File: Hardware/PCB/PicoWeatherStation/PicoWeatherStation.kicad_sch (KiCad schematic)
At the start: 42 parts, among them J1 TOUCH_PANEL, J2 LCD_BL, Q1 AO3400A, SW1 SW_PICO_RST, U1 Pico, U2 XPT2046

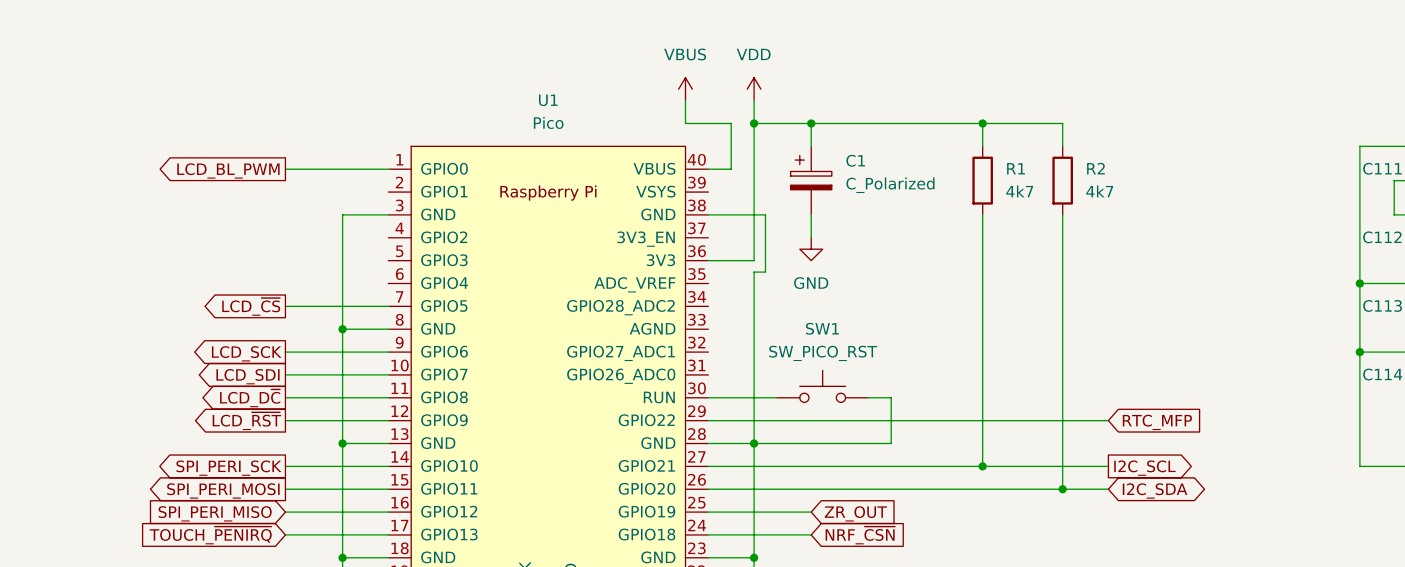
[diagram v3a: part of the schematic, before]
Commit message: PCB: wire-up the keyboard
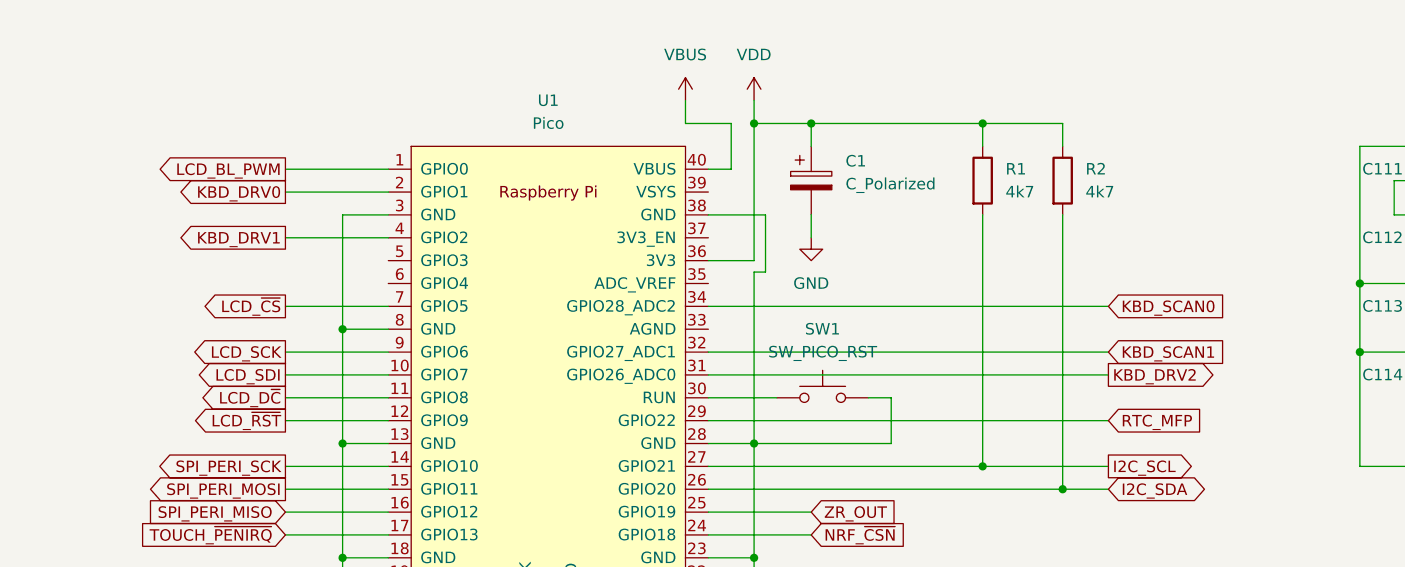
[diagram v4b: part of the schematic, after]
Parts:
- U1: footprint RPi_Pico:RPi_Pico_SMD -> PicoWeatherStation:RPi_PicoW_SMD
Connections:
- net KBD_DRV0: now reaches U1.2 (GPIO1)
- net KBD_DRV2: now reaches U1.31 (GPIO26_ADC0)
- net KBD_SCAN1: now reaches U1.32 (GPIO27_ADC1)
- net KBD_SCAN0: now reaches U1.34 (GPIO28_ADC2)
- net KBD_DRV1: now reaches U1.4 (GPIO2)
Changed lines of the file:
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@@
+    (stroke (width 0) (type default) (color 0 0 0 0))
+  )
+  (wire (pts (xy 59.69 123.19) (xy 71.12 123.19))
     (stroke (width 0) (type default) (color 0 0 0 0))
   )
@@
     (stroke (width 0) (type default) (color 0 0 0 0))
   )
+  (wire (pts (xy 106.68 130.81) (xy 151.13 130.81))
+    (stroke (width 0) (type default) (color 0 0 0 0))
+  )
   (wire (pts (xy 252.73 105.41) (xy 257.81 105.41))
     (stroke (width 0) (type default) (color 0 0 0 0))
@@
     (stroke (width 0) (type default) (color 0 0 0 0))
   )
+  (wire (pts (xy 106.68 138.43) (xy 151.13 138.43))
+    (stroke (width 0) (type default) (color 0 0 0 0))
+  )
+  (wire (pts (xy 59.69 118.11) (xy 71.12 118.11))
+    (stroke (width 0) (type default) (color 0 0 0 0))
+  )
   (wire (pts (xy 184.15 53.34) (xy 191.77 53.34))
     (stroke (width 0) (type default) (color 0 0 0 0))
@@
   )
   (wire (pts (xy 238.76 77.47) (xy 238.76 97.79))
+    (stroke (width 0) (type default) (color 0 0 0 0))
+  )
+  (wire (pts (xy 106.68 135.89) (xy 151.13 135.89))
     (stroke (width 0) (type default) (color 0 0 0 0))
   )
@@
     (property "Intersheet References" "${INTERSHEET_REFS}" (id 0) (at 161.1631 151.0506 0)
       (effects (font (size 1.27 1.27)) (justify left) hide)
+    )
+  )
+  (global_label "KBD_DRV1" (shape output) (at 59.69 123.19 180) (fields_autoplaced)
+    (effects (font (size 1.27 1.27)) (justify right))
+    (property "Intersheet References" "${INTERSHEET_REFS}" (id 0) (at 47.6612 123.1106 0)
+      (effects (font (size 1.27 1.27)) (justify right) hide)
     )
   )
@@
     )
   )
+  (global_label "KBD_SCAN0" (shape input) (at 151.13 130.81 0) (fields_autoplaced)
+    (effects (font (size 1.27 1.27)) (justify left))
+    (property "Intersheet References" "${INTERSHEET_REFS}" (id 0) (at 164.4288 130.7306 0)
+      (effects (font (size 1.27 1.27)) (justify left) hide)
+    )
+  )
   (global_label "LCD_V0" (shape passive) (at 208.28 113.03 90) (fields_autoplaced)
     (effects (font (size 1.27 1.27)) (justify left))
@@
     )
   )
+  (global_label "KBD_DRV0" (shape output) (at 59.69 118.11 180) (fields_autoplaced)
+    (effects (font (size 1.27 1.27)) (justify right))
+    (property "Intersheet References" "${INTERSHEET_REFS}" (id 0) (at 47.6612 118.0306 0)
+      (effects (font (size 1.27 1.27)) (justify right) hide)
+    )
+  )
   (global_label "LCD_~{RST}" (shape output) (at 59.69 143.51 180) (fields_autoplaced)
     (effects (font (size 1.27 1.27)) (justify right))
@@
     )
   )
+  (global_label "KBD_DRV2" (shape output) (at 151.13 138.43 0) (fields_autoplaced)
+    (effects (font (size 1.27 1.27)) (justify left))
+    (property "Intersheet References" "${INTERSHEET_REFS}" (id 0) (at 163.1588 138.3506 0)
+      (effects (font (size 1.27 1.27)) (justify left) hide)
+    )
+  )
   (global_label "SPI_PERI_MOSI" (shape input) (at 111.76 49.53 0) (fields_autoplaced)
     (effects (font (size 1.27 1.27)) (justify left))
@@
     (effects (font (size 1.27 1.27)) (justify left))
     (property "Intersheet References" "${INTERSHEET_REFS}" (id 0) (at 278.6683 128.1906 0)
+      (effects (font (size 1.27 1.27)) (justify left) hide)
+    )
+  )
+  (global_label "KBD_SCAN1" (shape input) (at 151.13 135.89 0) (fields_autoplaced)
+    (effects (font (size 1.27 1.27)) (justify left))
+    (property "Intersheet References" "${INTERSHEET_REFS}" (id 0) (at 164.4288 135.8106 0)
       (effects (font (size 1.27 1.27)) (justify left) hide)
     )
@@
     (property "Reference" "U1" (id 0) (at 88.9 107.95 0))
     (property "Value" "Pico" (id 1) (at 88.9 110.49 0))
-    (property "Footprint" "RPi_Pico:RPi_Pico_SMD" (id 2) (at 88.9 139.7 90)
+    (property "Footprint" "PicoWeatherStation:RPi_PicoW_SMD" (id 2) (at 88.9 139.7 90)
       (effects (font (size 1.27 1.27)) hide)
     )
@@
     )
     (path "/8427f957-6735-4f61-a9c3-6b6f45bea61c"
-      (reference "U1") (unit 1) (value "Pico") (footprint "RPi_Pico:RPi_Pico_SMD")
+      (reference "U1") (unit 1) (value "Pico") (footprint "PicoWeatherStation:RPi_PicoW_SMD")
     )
     (path "/540f484c-d60b-45a7-9525-536c50565709"

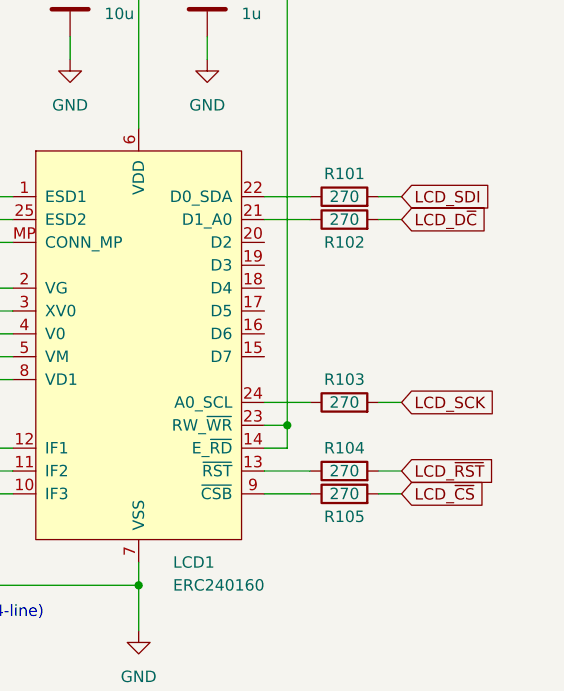
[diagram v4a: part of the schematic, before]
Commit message: PCB: optimize high speed LCD signal tracks
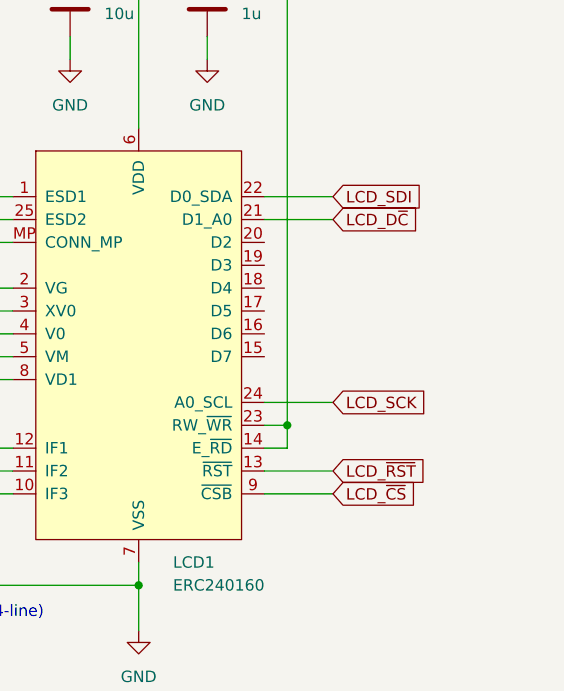
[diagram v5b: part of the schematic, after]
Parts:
- removed R101, R102, R103, R104, R105: 270, Resistor_SMD:R_0805_2012Metric_Pad1.20x1.40mm_HandSolder, symbol Device:R
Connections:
- net LCD_D~{C}: now also LCD1.21 (D1_A0)
- net LCD_SCK: now also LCD1.24 (A0_SCL)
- net LCD_SDI: now also LCD1.22 (D0_SDA)
- net LCD_~{CS}: now also LCD1.9 (~{CSB})
- net LCD_~{RST}: now also LCD1.13 (~{RST})
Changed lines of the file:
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@@
-    (stroke (width 0) (type default) (color 0 0 0 0))
-  )
-  (wire (pts (xy 265.43 107.95) (xy 267.97 107.95))
     (stroke (width 0) (type default) (color 0 0 0 0))
   )
@@
     (stroke (width 0) (type default) (color 0 0 0 0))
   )
-  (wire (pts (xy 252.73 107.95) (xy 257.81 107.95))
+  (wire (pts (xy 252.73 107.95) (xy 260.35 107.95))
     (stroke (width 0) (type default) (color 0 0 0 0))
   )
@@
     (stroke (width 0) (type default) (color 0 0 0 0))
   )
-  (wire (pts (xy 252.73 138.43) (xy 257.81 138.43))
+  (wire (pts (xy 252.73 138.43) (xy 260.35 138.43))
     (stroke (width 0) (type default) (color 0 0 0 0))
   )
@@
     (stroke (width 0) (type default) (color 0 0 0 0))
   )
-  (wire (pts (xy 265.43 128.27) (xy 267.97 128.27))
-    (stroke (width 0) (type default) (color 0 0 0 0))
-  )
   (wire (pts (xy 106.68 151.13) (xy 146.05 151.13))
     (stroke (width 0) (type default) (color 0 0 0 0))
@@
     (stroke (width 0) (type default) (color 0 0 0 0))
   )
-  (wire (pts (xy 265.43 138.43) (xy 267.97 138.43))
-    (stroke (width 0) (type default) (color 0 0 0 0))
-  )
   (wire (pts (xy 111.76 127) (xy 111.76 146.05))
     (stroke (width 0) (type default) (color 0 0 0 0))
@@
     (stroke (width 0) (type default) (color 0 0 0 0))
   )
-  (wire (pts (xy 252.73 128.27) (xy 257.81 128.27))
+  (wire (pts (xy 252.73 128.27) (xy 260.35 128.27))
     (stroke (width 0) (type default) (color 0 0 0 0))
   )
@@
     (stroke (width 0) (type default) (color 0 0 0 0))
   )
-  (wire (pts (xy 265.43 135.89) (xy 267.97 135.89))
-    (stroke (width 0) (type default) (color 0 0 0 0))
-  )
   (wire (pts (xy 113.03 120.65) (xy 113.03 127))
     (stroke (width 0) (type default) (color 0 0 0 0))
@@
     (stroke (width 0) (type default) (color 0 0 0 0))
   )
-  (wire (pts (xy 252.73 105.41) (xy 257.81 105.41))
-    (stroke (width 0) (type default) (color 0 0 0 0))
-  )
   (wire (pts (xy 69.85 22.86) (xy 69.85 25.4))
     (stroke (width 0) (type default) (color 0 0 0 0))
@@
     (stroke (width 0) (type default) (color 0 0 0 0))
   )
-  (wire (pts (xy 252.73 135.89) (xy 257.81 135.89))
+  (wire (pts (xy 252.73 135.89) (xy 260.35 135.89))
     (stroke (width 0) (type default) (color 0 0 0 0))
   )
@@
     (stroke (width 0) (type default) (color 0 0 0 0))
   )
-  (wire (pts (xy 265.43 105.41) (xy 267.97 105.41))
+  (wire (pts (xy 252.73 105.41) (xy 260.35 105.41))
     (stroke (width 0) (type default) (color 0 0 0 0))
   )
@@
     )
   )
-  (global_label "LCD_~{CS}" (shape input) (at 267.97 138.43 0) (fields_autoplaced)
-    (effects (font (size 1.27 1.27)) (justify left))
-    (property "Intersheet References" "${INTERSHEET_REFS}" (id 0) (at 277.3983 138.3506 0)
+  (global_label "LCD_~{CS}" (shape input) (at 260.35 138.43 0) (fields_autoplaced)
+    (effects (font (size 1.27 1.27)) (justify left))
+    (property "Intersheet References" "${INTERSHEET_REFS}" (id 0) (at 269.7783 138.3506 0)
       (effects (font (size 1.27 1.27)) (justify left) hide)
     )
@@
     )
   )
-  (global_label "LCD_D~{C}" (shape input) (at 267.97 107.95 0) (fields_autoplaced)
-    (effects (font (size 1.27 1.27)) (justify left))
-    (property "Intersheet References" "${INTERSHEET_REFS}" (id 0) (at 277.4588 107.8706 0)
+  (global_label "LCD_D~{C}" (shape input) (at 260.35 107.95 0) (fields_autoplaced)
+    (effects (font (size 1.27 1.27)) (justify left))
+    (property "Intersheet References" "${INTERSHEET_REFS}" (id 0) (at 269.8388 107.8706 0)
       (effects (font (size 1.27 1.27)) (justify left) hide)
     )
@@
     )
   )
-  (global_label "LCD_~{RST}" (shape input) (at 267.97 135.89 0) (fields_autoplaced)
-    (effects (font (size 1.27 1.27)) (justify left))
-    (property "Intersheet References" "${INTERSHEET_REFS}" (id 0) (at 278.366 135.8106 0)
+  (global_label "LCD_~{RST}" (shape input) (at 260.35 135.89 0) (fields_autoplaced)
+    (effects (font (size 1.27 1.27)) (justify left))
+    (property "Intersheet References" "${INTERSHEET_REFS}" (id 0) (at 270.746 135.8106 0)
       (effects (font (size 1.27 1.27)) (justify left) hide)
     )
@@
     )
   )
-  (global_label "LCD_SDI" (shape input) (at 267.97 105.41 0) (fields_autoplaced)
-    (effects (font (size 1.27 1.27)) (justify left))
-    (property "Intersheet References" "${INTERSHEET_REFS}" (id 0) (at 278.0031 105.3306 0)
-      (effects (font (size 1.27 1.27)) (justify left) hide)
-    )
-  )
-  (global_label "LCD_SCK" (shape input) (at 267.97 128.27 0) (fields_autoplaced)
-    (effects (font (size 1.27 1.27)) (justify left))
-    (property "Intersheet References" "${INTERSHEET_REFS}" (id 0) (at 278.6683 128.1906 0)
+  (global_label "LCD_SDI" (shape input) (at 260.35 105.41 0) (fields_autoplaced)
+    (effects (font (size 1.27 1.27)) (justify left))
+    (property "Intersheet References" "${INTERSHEET_REFS}" (id 0) (at 270.3831 105.3306 0)
+      (effects (font (size 1.27 1.27)) (justify left) hide)
+    )
+  )
+  (global_label "LCD_SCK" (shape input) (at 260.35 128.27 0) (fields_autoplaced)
+    (effects (font (size 1.27 1.27)) (justify left))
+    (property "Intersheet References" "${INTERSHEET_REFS}" (id 0) (at 271.0483 128.1906 0)
       (effects (font (size 1.27 1.27)) (justify left) hide)
     )
@@
     )
   )
-  (symbol (lib_id "Device:R") (at 261.62 107.95 90) (unit 1)
-    (in_bom yes) (on_board yes)
-    (property "Reference" "R102" (id 0) (at 261.62 110.49 90))
-    (property "Value" "270" (id 1) (at 261.62 107.95 90))
-    (property "Footprint" "Resistor_SMD:R_0805_2012Metric_Pad1.20x1.40mm_HandSolder" (id 2) (at 261.62 109.728 90)
-      (effects (font (size 1.27 1.27)) hide)
-    )
-    (property "Datasheet" "~" (id 3) (at 261.62 107.95 0)
-      (effects (font (size 1.27 1.27)) hide)
-    )
-    (pin "1")
-    (pin "2")
-  )
   (symbol (lib_id "Device:C") (at 189.23 113.03 90) (unit 1)
     (in_bom yes) (on_board yes)
@@
     (pin "2")
   )
-  (symbol (lib_id "Device:R") (at 261.62 138.43 90) (unit 1)
-    (in_bom yes) (on_board yes)
-    (property "Reference" "R105" (id 0) (at 261.62 140.97 90))
-    (property "Value" "270" (id 1) (at 261.62 138.43 90))
-    (property "Footprint" "Resistor_SMD:R_0805_2012Metric_Pad1.20x1.40mm_HandSolder" (id 2) (at 261.62 140.208 90)
-      (effects (font (size 1.27 1.27)) hide)
-    )
-    (property "Datasheet" "~" (id 3) (at 261.62 138.43 0)
-      (effects (font (size 1.27 1.27)) hide)
-    )
-    (pin "1")
-    (pin "2")
-  )
   (symbol (lib_id "Device:C") (at 44.45 31.75 0) (unit 1)
     (in_bom yes) (on_board yes)
@@
     )
     (pin "1")
-  )
-  (symbol (lib_id "Device:R") (at 261.62 135.89 90) (unit 1)
-    (in_bom yes) (on_board yes)
-    (property "Reference" "R104" (id 0) (at 261.62 133.35 90))
-    (property "Value" "270" (id 1) (at 261.62 135.89 90))
-    (property "Footprint" "Resistor_SMD:R_0805_2012Metric_Pad1.20x1.40mm_HandSolder" (id 2) (at 261.62 137.668 90)
-      (effects (font (size 1.27 1.27)) hide)
-    )
-    (property "Datasheet" "~" (id 3) (at 261.62 135.89 0)
-      (effects (font (size 1.27 1.27)) hide)
-    )
-    (pin "1")
-    (pin "2")
   )
   (symbol (lib_id "power:GND") (at 246.38 90.17 0) (unit 1)
@@
     (pin "3")
     (pin "4")
-  )
-  (symbol (lib_id "Device:R") (at 261.62 128.27 90) (unit 1)
-    (in_bom yes) (on_board yes)
-    (property "Reference" "R103" (id 0) (at 261.62 125.73 90))
-    (property "Value" "270" (id 1) (at 261.62 128.27 90))
-    (property "Footprint" "Resistor_SMD:R_0805_2012Metric_Pad1.20x1.40mm_HandSolder" (id 2) (at 261.62 130.048 90)
-      (effects (font (size 1.27 1.27)) hide)
-    )
-    (property "Datasheet" "~" (id 3) (at 261.62 128.27 0)
-      (effects (font (size 1.27 1.27)) hide)
-    )
-    (pin "1")
-    (pin "2")
   )
   (symbol (lib_id "Device:R") (at 90.17 52.07 90) (unit 1)
@@
     (pin "2")
   )
-  (symbol (lib_id "Device:R") (at 261.62 105.41 90) (unit 1)
-    (in_bom yes) (on_board yes)
-    (property "Reference" "R101" (id 0) (at 261.62 102.87 90))
-    (property "Value" "270" (id 1) (at 261.62 105.41 90))
-    (property "Footprint" "Resistor_SMD:R_0805_2012Metric_Pad1.20x1.40mm_HandSolder" (id 2) (at 261.62 107.188 90)
-      (effects (font (size 1.27 1.27)) hide)
-    )
-    (property "Datasheet" "~" (id 3) (at 261.62 105.41 0)
-      (effects (font (size 1.27 1.27)) hide)
-    )
-    (pin "1")
-    (pin "2")
-  )
   (symbol (lib_id "Device:C_Polarized") (at 118.11 116.84 0) (unit 1)
     (in_bom yes) (on_board yes) (fields_autoplaced)
@@
       (reference "R2") (unit 1) (value "4k7") (footprint "Resistor_SMD:R_0805_2012Metric_Pad1.20x1.40mm_HandSolder")
     )
-    (path "/ad11c5bf-60b1-48a2-96aa-93c193b76938"
-      (reference "R101") (unit 1) (value "270") (footprint "Resistor_SMD:R_0805_2012Metric_Pad1.20x1.40mm_HandSolder")
-    )
-    (path "/25832b5b-c098-49ae-bc36-e9ef6ab620d6"
-      (reference "R102") (unit 1) (value "270") (footprint "Resistor_SMD:R_0805_2012Metric_Pad1.20x1.40mm_HandSolder")
-    )
-    (path "/6f567f0f-78a8-4486-987d-58dde60f5f06"
-      (reference "R103") (unit 1) (value "270") (footprint "Resistor_SMD:R_0805_2012Metric_Pad1.20x1.40mm_HandSolder")
-    )
-    (path "/481e9054-2c05-4540-956a-ea5bf16adcca"
-      (reference "R104") (unit 1) (value "270") (footprint "Resistor_SMD:R_0805_2012Metric_Pad1.20x1.40mm_HandSolder")
-    )
-    (path "/37d303ea-eb85-46c8-a409-8bb2e3892dd4"
-      (reference "R105") (unit 1) (value "270") (footprint "Resistor_SMD:R_0805_2012Metric_Pad1.20x1.40mm_HandSolder")
-    )
     (path "/8fdd9cf7-bac7-44c9-9bef-6a484f8265f6"

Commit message: PCB: prepare for manufacturing
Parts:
- added R208: 100k, Resistor_SMD:R_0805_2012Metric_Pad1.20x1.40mm_HandSolder, symbol Device:R
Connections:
- net GND: now also U1.33 (AGND)
- net TOUCH_~{CS}: now also R208.2
- net VDD: now also R208.1
